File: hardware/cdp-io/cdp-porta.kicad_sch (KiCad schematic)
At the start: 5 parts, among them U1 74LS573, U2 74LS573, U3 74LS00

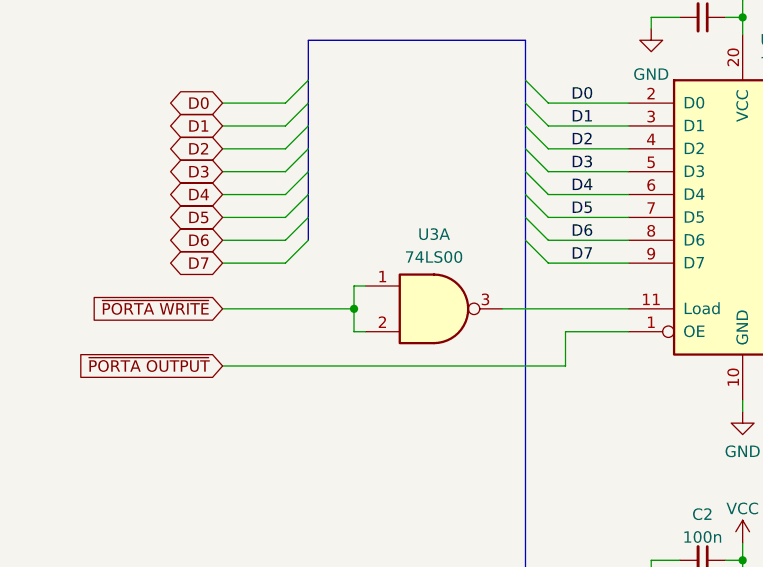
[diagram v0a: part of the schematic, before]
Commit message: The controller is finished. U7 is changed to a hex inverter.
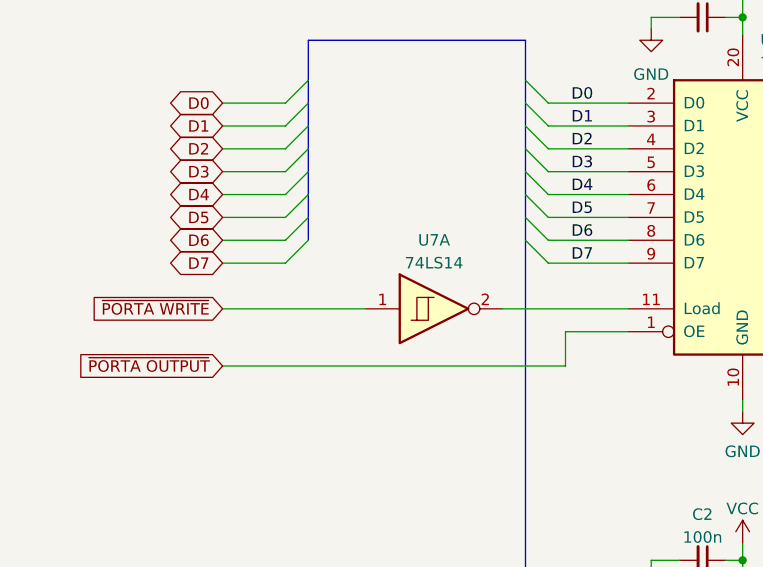
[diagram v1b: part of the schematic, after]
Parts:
- removed U3: 74LS00, Package_DIP:DIP-14_W7.62mm_Socket, symbol 74xx:74LS00
- added U7: 74LS14, symbol 74xx:74LS14
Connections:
- net ~{PORTA WRITE}: now also U7.1
- net at U1.11 (Load): now also U7.2
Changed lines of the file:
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@@
 (kicad_sch (version 20230121) (generator eeschema)
   (paper "A4")
-  (junction (at 112.395 65.405) (diameter 0) (color 0 0 0 0)
-  )
   (junction (at 155.575 93.345) (diameter 0) (color 0 0 0 0)
   )
@@
     (stroke (width 0) (type default))
   )
-  (wire (pts (xy 97.79 65.405) (xy 112.395 65.405))
-    (stroke (width 0) (type default))
-  )
   (bus (pts (xy 131.445 42.545) (xy 131.445 40.005))
     (stroke (width 0) (type default))
@@
     (stroke (width 0) (type default))
   )
-  (wire (pts (xy 112.395 65.405) (xy 112.395 67.945))
-    (stroke (width 0) (type default))
-  )
   (bus (pts (xy 181.61 110.49) (xy 181.61 107.95))
     (stroke (width 0) (type default))
@@
     (stroke (width 0) (type default))
   )
+  (wire (pts (xy 97.79 65.405) (xy 113.665 65.405))
+    (stroke (width 0) (type default))
+  )
   (wire (pts (xy 208.915 55.245) (xy 216.535 55.245))
     (stroke (width 0) (type default))
@@
     (stroke (width 0) (type default))
   )
-  (wire (pts (xy 112.395 62.865) (xy 112.395 65.405))
-    (stroke (width 0) (type default))
-  )
   (bus (pts (xy 131.445 47.625) (xy 131.445 45.085))
     (stroke (width 0) (type default))
   )
-  (wire (pts (xy 112.395 67.945) (xy 113.665 67.945))
-    (stroke (width 0) (type default))
-  )
   (wire (pts (xy 145.415 33.02) (xy 145.415 34.29))
     (stroke (width 0) (type default))
@@
   )
   (wire (pts (xy 148.59 33.02) (xy 145.415 33.02))
-    (stroke (width 0) (type default))
-  )
-  (wire (pts (xy 113.665 62.865) (xy 112.395 62.865))
     (stroke (width 0) (type default))
   )
@@
         (path "/479e9a3e-8705-41df-8009-7e8503809f49/05095c2f-eeee-4b53-a55c-38329025afd6"
           (reference "C2") (unit 1)
-        )
-      )
-    )
-  )
-  (symbol (lib_id "74xx:74LS00") (at 121.285 65.405 0) (unit 1)
-    (in_bom yes) (on_board yes) (dnp no) (fields_autoplaced)
-    (property "Reference" "U3" (at 121.2767 57.15 0)
-      (effects (font (size 1.27 1.27)))
-    )
-    (property "Value" "74LS00" (at 121.2767 59.69 0)
-      (effects (font (size 1.27 1.27)))
-    )
-    (property "Footprint" "Package_DIP:DIP-14_W7.62mm_Socket" (at 121.285 65.405 0)
-      (effects (font (size 1.27 1.27)) hide)
-    )
-    (property "Datasheet" "http://www.ti.com/lit/gpn/sn74ls00" (at 121.285 65.405 0)
-      (effects (font (size 1.27 1.27)) hide)
-    )
-    (pin "1")
-    (pin "2")
-    (pin "3")
-    (pin "4")
-    (pin "5")
-    (pin "6")
-    (pin "10")
-    (pin "8")
-    (pin "9")
-    (pin "11")
-    (pin "12")
-    (pin "13")
-    (pin "14")
-    (pin "7")
-    (instances
-      (project "cdp-io"
-        (path "/479e9a3e-8705-41df-8009-7e8503809f49"
-          (reference "U3") (unit 1)
-        )
-        (path "/479e9a3e-8705-41df-8009-7e8503809f49/05095c2f-eeee-4b53-a55c-38329025afd6"
-          (reference "U7") (unit 1)
         )
       )
@@
         )
       )
+    )
+  )
+  (symbol (lib_id "74xx:74LS14") (at 121.285 65.405 0) (unit 1)
+    (in_bom yes) (on_board yes) (dnp no) (fields_autoplaced)
+    (property "Reference" "U7" (at 121.285 57.785 0)
+      (effects (font (size 1.27 1.27)))
+    )
+    (property "Value" "74LS14" (at 121.285 60.325 0)
+      (effects (font (size 1.27 1.27)))
+    )
+    (property "Footprint" "" (at 121.285 65.405 0)
+      (effects (font (size 1.27 1.27)) hide)
+    )
+    (property "Datasheet" "http://www.ti.com/lit/gpn/sn74LS14" (at 121.285 65.405 0)
+      (effects (font (size 1.27 1.27)) hide)
+    )
+    (pin "1")
+    (pin "2")
+    (pin "3")
+    (pin "4")
+    (pin "5")
+    (pin "6")
+    (pin "8")
+    (pin "9")
+    (pin "10")
+    (pin "11")
+    (pin "12")
+    (pin "13")
+    (pin "14")
+    (pin "7")
+    (instances
+      (project "cdp-io"
+        (path "/479e9a3e-8705-41df-8009-7e8503809f49/fc5dd19a-450f-4ce7-af21-025e7154e993"
+          (reference "U7") (unit 1)
+        )
+        (path "/479e9a3e-8705-41df-8009-7e8503809f49/05095c2f-eeee-4b53-a55c-38329025afd6"
+          (reference "U7") (unit 1)
+        )
+      )

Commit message: Changed the layout a bit, started to work on the PCB.
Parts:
- U7: footprint (none) -> Package_DIP:DIP-14_W7.62mm_Socket
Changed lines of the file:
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@@
       (effects (font (size 1.27 1.27)))
     )
-    (property "Footprint" "" (at 121.285 65.405 0)
+    (property "Footprint" "Package_DIP:DIP-14_W7.62mm_Socket" (at 121.285 65.405 0)
       (effects (font (size 1.27 1.27)) hide)
     )

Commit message: Changed the schematic a bit.
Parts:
- removed U7: 74LS14, Package_DIP:DIP-14_W7.62mm_Socket, symbol 74xx:74LS14
- added U7: 74LS14, Package_DIP:DIP-14_W7.62mm_Socket, symbol 74xx:74LS14
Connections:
- net ~{PORTA WRITE}: now also U7.13
- net at U1.11 (Load): now also U7.12
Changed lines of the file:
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@@
     )
   )
-  (symbol (lib_id "power:GND") (at 145.415 94.615 0) (unit 1)
+  (symbol (lib_id "74xx:74LS14") (at 121.285 65.405 0) (unit 6)
     (in_bom yes) (on_board yes) (dnp no) (fields_autoplaced)
-    (property "Reference" "#PWR010" (at 145.415 100.965 0)
-      (effects (font (size 1.27 1.27)) hide)
-    )
-    (property "Value" "GND" (at 145.415 99.695 0)
+    (property "Reference" "U7" (at 121.285 57.15 0)
       (effects (font (size 1.27 1.27)))
     )
-    (property "Footprint" "" (at 145.415 94.615 0)
-      (effects (font (size 1.27 1.27)) hide)
-    )
-    (property "Datasheet" "" (at 145.415 94.615 0)
-      (effects (font (size 1.27 1.27)) hide)
-    )
-    (pin "1")
-    (instances
-      (project "cdp-io"
-        (path "/479e9a3e-8705-41df-8009-7e8503809f49/05095c2f-eeee-4b53-a55c-38329025afd6"
-          (reference "#PWR010") (unit 1)
-        )
-      )
-    )
-  )
-  (symbol (lib_id "74xx:74LS14") (at 121.285 65.405 0) (unit 1)
-    (in_bom yes) (on_board yes) (dnp no) (fields_autoplaced)
-    (property "Reference" "U7" (at 121.285 57.785 0)
-      (effects (font (size 1.27 1.27)))
-    )
-    (property "Value" "74LS14" (at 121.285 60.325 0)
+    (property "Value" "74LS14" (at 121.285 59.69 0)
       (effects (font (size 1.27 1.27)))
     )
@@
       (project "cdp-io"
         (path "/479e9a3e-8705-41df-8009-7e8503809f49/fc5dd19a-450f-4ce7-af21-025e7154e993"
-          (reference "U7") (unit 1)
+          (reference "U7") (unit 6)
         )
         (path "/479e9a3e-8705-41df-8009-7e8503809f49/05095c2f-eeee-4b53-a55c-38329025afd6"
-          (reference "U7") (unit 1)
+          (reference "U7") (unit 6)
         )
       )
+    )
+  )
+  (symbol (lib_id "power:GND") (at 145.415 94.615 0) (unit 1)
+    (in_bom yes) (on_board yes) (dnp no) (fields_autoplaced)
+    (property "Reference" "#PWR010" (at 145.415 100.965 0)
+      (effects (font (size 1.27 1.27)) hide)
+    )
+    (property "Value" "GND" (at 145.415 99.695 0)
+      (effects (font (size 1.27 1.27)))
+    )
+    (property "Footprint" "" (at 145.415 94.615 0)
+      (effects (font (size 1.27 1.27)) hide)
+    )
+    (property "Datasheet" "" (at 145.415 94.615 0)
+      (effects (font (size 1.27 1.27)) hide)
+    )
+    (pin "1")
+    (instances
+      (project "cdp-io"
+        (path "/479e9a3e-8705-41df-8009-7e8503809f49/05095c2f-eeee-4b53-a55c-38329025afd6"
+          (reference "#PWR010") (unit 1)
+        )
+      )

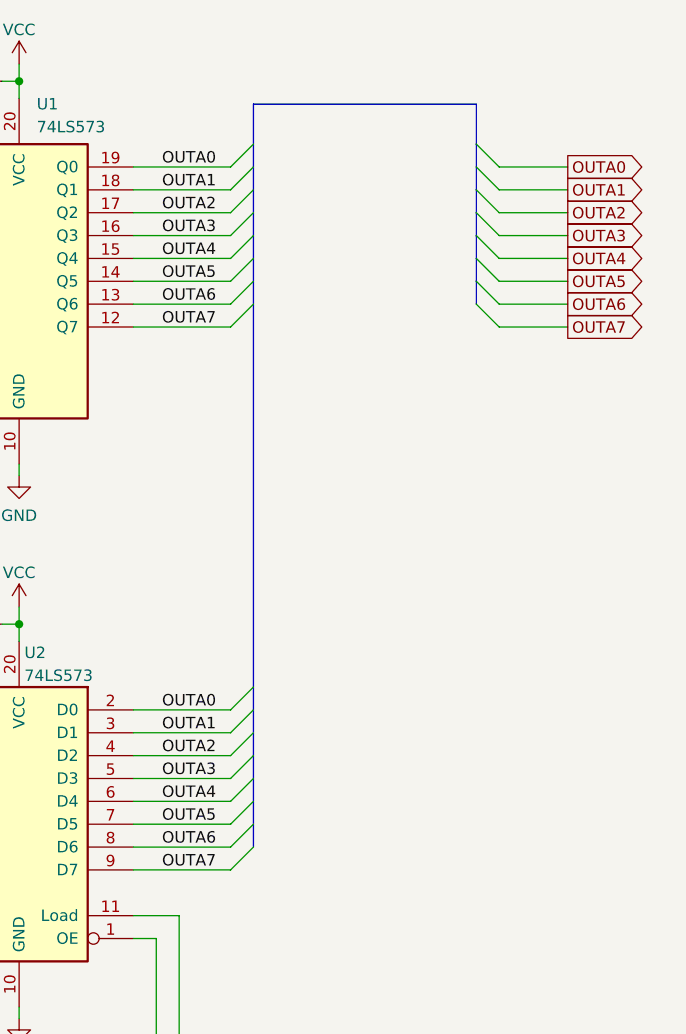
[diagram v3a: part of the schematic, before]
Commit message: Renamed a few net, and changed the schematic a bit. The PCB is ready!
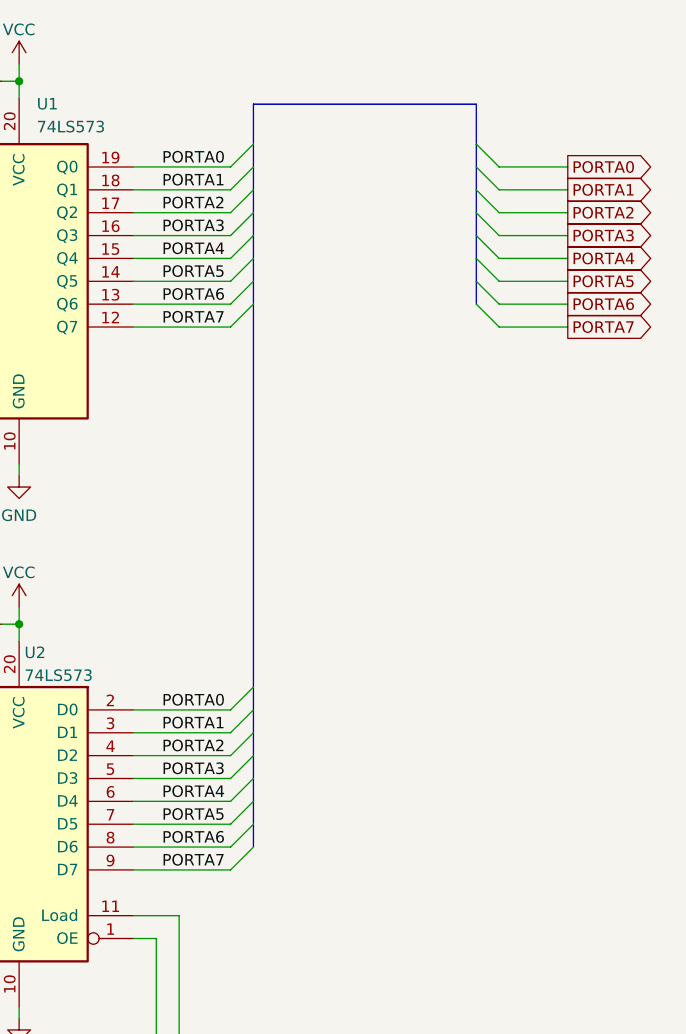
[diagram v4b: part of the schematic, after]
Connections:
- net OUTA0 renamed PORTA0
- net OUTA1 renamed PORTA1
- net OUTA2 renamed PORTA2
- net OUTA3 renamed PORTA3
- net OUTA4 renamed PORTA4
- net OUTA5 renamed PORTA5
- net OUTA6 renamed PORTA6
- net OUTA7 renamed PORTA7
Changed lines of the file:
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@@
     (effects (font (size 1.27 1.27)) (justify left bottom))
   )
-  (label "OUTA0" (at 171.45 42.545 0) (fields_autoplaced)
-    (effects (font (size 1.27 1.27)) (justify left bottom))
-  )
-  (label "OUTA2" (at 171.45 47.625 0) (fields_autoplaced)
-    (effects (font (size 1.27 1.27)) (justify left bottom))
-  )
-  (label "OUTA0" (at 171.45 102.87 0) (fields_autoplaced)
-    (effects (font (size 1.27 1.27)) (justify left bottom))
-  )
-  (label "OUTA4" (at 171.45 52.705 0) (fields_autoplaced)
+  (label "PORTA0" (at 171.45 42.545 0) (fields_autoplaced)
+    (effects (font (size 1.27 1.27)) (justify left bottom))
+  )
+  (label "PORTA2" (at 171.45 47.625 0) (fields_autoplaced)
+    (effects (font (size 1.27 1.27)) (justify left bottom))
+  )
+  (label "PORTA0" (at 171.45 102.87 0) (fields_autoplaced)
+    (effects (font (size 1.27 1.27)) (justify left bottom))
+  )
+  (label "PORTA4" (at 171.45 52.705 0) (fields_autoplaced)
     (effects (font (size 1.27 1.27)) (justify left bottom))
   )
@@
     (effects (font (size 1.27 1.27)) (justify left bottom))
   )
-  (label "OUTA7" (at 171.45 120.65 0) (fields_autoplaced)
-    (effects (font (size 1.27 1.27)) (justify left bottom))
-  )
-  (label "OUTA1" (at 171.45 45.085 0) (fields_autoplaced)
-    (effects (font (size 1.27 1.27)) (justify left bottom))
-  )
-  (label "OUTA4" (at 171.45 113.03 0) (fields_autoplaced)
+  (label "PORTA7" (at 171.45 120.65 0) (fields_autoplaced)
+    (effects (font (size 1.27 1.27)) (justify left bottom))
+  )
+  (label "PORTA1" (at 171.45 45.085 0) (fields_autoplaced)
+    (effects (font (size 1.27 1.27)) (justify left bottom))
+  )
+  (label "PORTA4" (at 171.45 113.03 0) (fields_autoplaced)
     (effects (font (size 1.27 1.27)) (justify left bottom))
   )
@@
     (effects (font (size 1.27 1.27)) (justify left bottom))
   )
-  (label "OUTA2" (at 171.45 107.95 0) (fields_autoplaced)
+  (label "PORTA2" (at 171.45 107.95 0) (fields_autoplaced)
     (effects (font (size 1.27 1.27)) (justify left bottom))
   )
@@
     (effects (font (size 1.27 1.27)) (justify left bottom))
   )
-  (label "OUTA1" (at 171.45 105.41 0) (fields_autoplaced)
+  (label "PORTA1" (at 171.45 105.41 0) (fields_autoplaced)
     (effects (font (size 1.27 1.27)) (justify left bottom))
   )
@@
     (effects (font (size 1.27 1.27)) (justify left bottom))
   )
-  (label "OUTA5" (at 171.45 55.245 0) (fields_autoplaced)
-    (effects (font (size 1.27 1.27)) (justify left bottom))
-  )
-  (label "OUTA3" (at 171.45 110.49 0) (fields_autoplaced)
+  (label "PORTA5" (at 171.45 55.245 0) (fields_autoplaced)
+    (effects (font (size 1.27 1.27)) (justify left bottom))
+  )
+  (label "PORTA3" (at 171.45 110.49 0) (fields_autoplaced)
     (effects (font (size 1.27 1.27)) (justify left bottom))
   )
@@
     (effects (font (size 1.27 1.27)) (justify left bottom))
   )
-  (label "OUTA6" (at 171.45 118.11 0) (fields_autoplaced)
-    (effects (font (size 1.27 1.27)) (justify left bottom))
-  )
-  (label "OUTA5" (at 171.45 115.57 0) (fields_autoplaced)
+  (label "PORTA6" (at 171.45 118.11 0) (fields_autoplaced)
+    (effects (font (size 1.27 1.27)) (justify left bottom))
+  )
+  (label "PORTA5" (at 171.45 115.57 0) (fields_autoplaced)
     (effects (font (size 1.27 1.27)) (justify left bottom))
   )
@@
     (effects (font (size 1.27 1.27)) (justify left bottom))
   )
-  (label "OUTA6" (at 171.45 57.785 0) (fields_autoplaced)
+  (label "PORTA6" (at 171.45 57.785 0) (fields_autoplaced)
     (effects (font (size 1.27 1.27)) (justify left bottom))
   )
@@
     (effects (font (size 1.27 1.27)) (justify left bottom))
   )
-  (label "OUTA7" (at 171.45 60.325 0) (fields_autoplaced)
-    (effects (font (size 1.27 1.27)) (justify left bottom))
-  )
-  (label "OUTA3" (at 171.45 50.165 0) (fields_autoplaced)
-    (effects (font (size 1.27 1.27)) (justify left bottom))
-  )
-  (global_label "OUTA7" (shape output) (at 216.535 60.325 0) (fields_autoplaced)
-    (effects (font (size 1.27 1.27)) (justify left))
-    (property "Intersheetrefs" "${INTERSHEET_REFS}" (at 225.3675 60.325 0)
+  (label "PORTA7" (at 171.45 60.325 0) (fields_autoplaced)
+    (effects (font (size 1.27 1.27)) (justify left bottom))
+  )
+  (label "PORTA3" (at 171.45 50.165 0) (fields_autoplaced)
+    (effects (font (size 1.27 1.27)) (justify left bottom))
+  )
+  (global_label "PORTA7" (shape output) (at 216.535 60.325 0) (fields_autoplaced)
+    (effects (font (size 1.27 1.27)) (justify left))
+    (property "Intersheetrefs" "${INTERSHEET_REFS}" (at 226.577 60.325 0)
       (effects (font (size 1.27 1.27)) (justify left) hide)
     )
@@
     )
   )
-  (global_label "OUTA2" (shape output) (at 216.535 47.625 0) (fields_autoplaced)
-    (effects (font (size 1.27 1.27)) (justify left))
-    (property "Intersheetrefs" "${INTERSHEET_REFS}" (at 225.3675 47.625 0)
-      (effects (font (size 1.27 1.27)) (justify left) hide)
-    )
-  )
-  (global_label "OUTA4" (shape output) (at 216.535 52.705 0) (fields_autoplaced)
-    (effects (font (size 1.27 1.27)) (justify left))
-    (property "Intersheetrefs" "${INTERSHEET_REFS}" (at 225.3675 52.705 0)
+  (global_label "PORTA2" (shape output) (at 216.535 47.625 0) (fields_autoplaced)
+    (effects (font (size 1.27 1.27)) (justify left))
+    (property "Intersheetrefs" "${INTERSHEET_REFS}" (at 226.577 47.625 0)
+      (effects (font (size 1.27 1.27)) (justify left) hide)
+    )
+  )
+  (global_label "PORTA4" (shape output) (at 216.535 52.705 0) (fields_autoplaced)
+    (effects (font (size 1.27 1.27)) (justify left))
+    (property "Intersheetrefs" "${INTERSHEET_REFS}" (at 226.577 52.705 0)
       (effects (font (size 1.27 1.27)) (justify left) hide)
     )
@@
     )
   )
-  (global_label "OUTA0" (shape output) (at 216.535 42.545 0) (fields_autoplaced)
-    (effects (font (size 1.27 1.27)) (justify left))
-    (property "Intersheetrefs" "${INTERSHEET_REFS}" (at 225.3675 42.545 0)
-      (effects (font (size 1.27 1.27)) (justify left) hide)
-    )
-  )
-  (global_label "OUTA5" (shape output) (at 216.535 55.245 0) (fields_autoplaced)
-    (effects (font (size 1.27 1.27)) (justify left))
-    (property "Intersheetrefs" "${INTERSHEET_REFS}" (at 225.3675 55.245 0)
-      (effects (font (size 1.27 1.27)) (justify left) hide)
-    )
-  )
-  (global_label "OUTA3" (shape output) (at 216.535 50.165 0) (fields_autoplaced)
-    (effects (font (size 1.27 1.27)) (justify left))
-    (property "Intersheetrefs" "${INTERSHEET_REFS}" (at 225.3675 50.165 0)
+  (global_label "PORTA0" (shape output) (at 216.535 42.545 0) (fields_autoplaced)
+    (effects (font (size 1.27 1.27)) (justify left))
+    (property "Intersheetrefs" "${INTERSHEET_REFS}" (at 226.577 42.545 0)
+      (effects (font (size 1.27 1.27)) (justify left) hide)
+    )
+  )
+  (global_label "PORTA5" (shape output) (at 216.535 55.245 0) (fields_autoplaced)
+    (effects (font (size 1.27 1.27)) (justify left))
+    (property "Intersheetrefs" "${INTERSHEET_REFS}" (at 226.577 55.245 0)
+      (effects (font (size 1.27 1.27)) (justify left) hide)
+    )
+  )
+  (global_label "PORTA3" (shape output) (at 216.535 50.165 0) (fields_autoplaced)
+    (effects (font (size 1.27 1.27)) (justify left))
+    (property "Intersheetrefs" "${INTERSHEET_REFS}" (at 226.577 50.165 0)
       (effects (font (size 1.27 1.27)) (justify left) hide)
     )
@@
     )
   )
-  (global_label "OUTA6" (shape output) (at 216.535 57.785 0) (fields_autoplaced)
-    (effects (font (size 1.27 1.27)) (justify left))
-    (property "Intersheetrefs" "${INTERSHEET_REFS}" (at 225.3675 57.785 0)
+  (global_label "PORTA6" (shape output) (at 216.535 57.785 0) (fields_autoplaced)
+    (effects (font (size 1.27 1.27)) (justify left))
+    (property "Intersheetrefs" "${INTERSHEET_REFS}" (at 226.577 57.785 0)
       (effects (font (size 1.27 1.27)) (justify left) hide)
     )
@@
     )
   )
-  (global_label "OUTA1" (shape output) (at 216.535 45.085 0) (fields_autoplaced)
-    (effects (font (size 1.27 1.27)) (justify left))
-    (property "Intersheetrefs" "${INTERSHEET_REFS}" (at 225.3675 45.085 0)
-      (effects (font (size 1.27 1.27)) (justify left) hide)
-    )
+  (global_label "PORTA1" (shape output) (at 216.535 45.085 0) (fields_autoplaced)
+    (effects (font (size 1.27 1.27)) (justify left))
+    (property "Intersheetrefs" "${INTERSHEET_REFS}" (at 226.577 45.085 0)
+      (effects (font (size 1.27 1.27)) (justify left) hide)
+    )

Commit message: The final version of the IO board. Gerber files added.
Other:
- company: (none) -> ZLED
- title: (none) -> Port A
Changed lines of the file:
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@@
 (kicad_sch (version 20230121) (generator eeschema)
   (paper "A4")
+  (title_block
+    (title "Port A")
+    (date "2023-07-06")
+    (rev "1")
+    (company "ZLED")
+  )
   (junction (at 155.575 93.345) (diameter 0) (color 0 0 0 0)
   )

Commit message: IC names fixed. PCB is updated. Gerber files are still ok.
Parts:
- U1, U2: value 74LS573 -> 74HC573
- U7: value 74LS14 -> 74HC14
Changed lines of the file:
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@@
       (effects (font (size 1.27 1.27)) (justify right))
     )
-    (property "Value" "74LS573" (at 156.1591 99.06 0)
+    (property "Value" "74HC573" (at 156.1591 99.06 0)
       (effects (font (size 1.27 1.27)) (justify right))
     )
@@
       (effects (font (size 1.27 1.27)) (justify left))
     )
-    (property "Value" "74LS573" (at 157.5309 38.1 0)
+    (property "Value" "74HC573" (at 157.5309 38.1 0)
       (effects (font (size 1.27 1.27)) (justify left))
     )
@@
       (effects (font (size 1.27 1.27)))
     )
-    (property "Value" "74LS14" (at 121.285 59.69 0)
+    (property "Value" "74HC14" (at 121.285 59.69 0)
       (effects (font (size 1.27 1.27)))
     )
